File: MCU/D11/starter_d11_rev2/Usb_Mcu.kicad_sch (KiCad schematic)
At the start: 14 parts, among them J1 USB_A, J2 Data, J3 SWD-5, SW1 Reset, U1 PRTR5V0, U2 ATSAMD11C14A-SS, X1 ECS-2520MV-xxx-xx

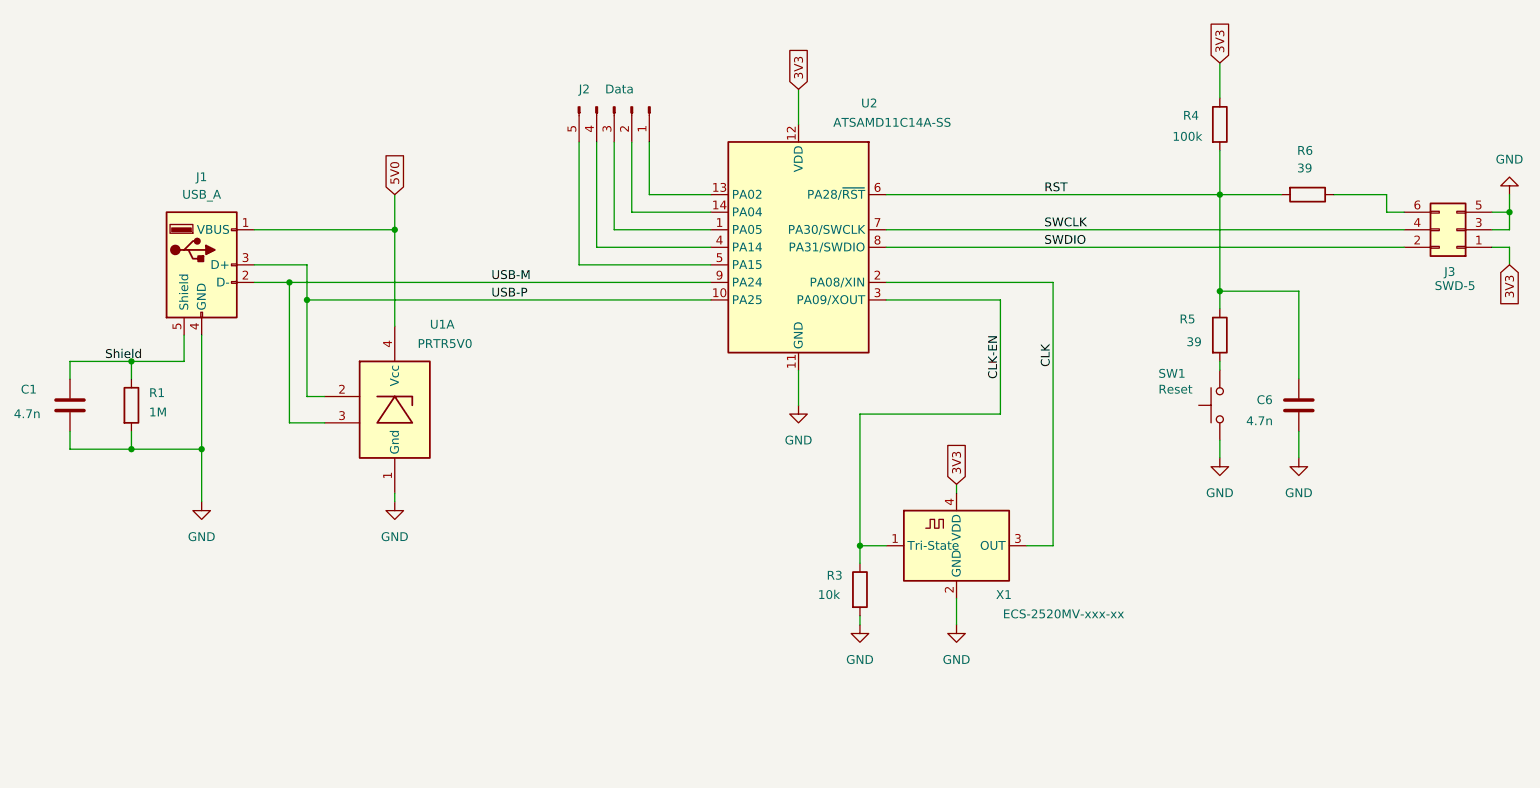
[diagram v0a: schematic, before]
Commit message: D11 schematics and PCB updates - printed prototype version
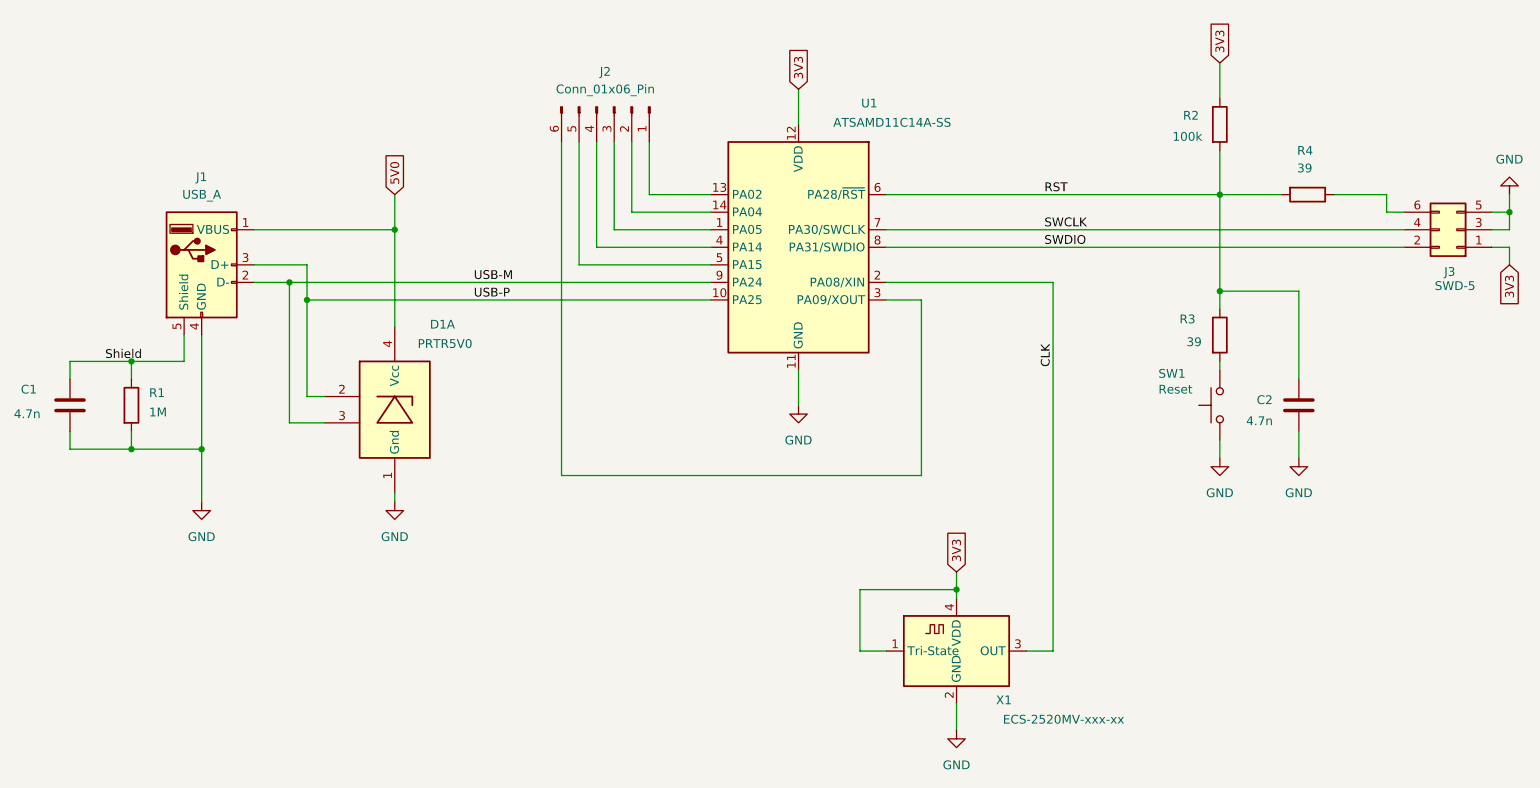
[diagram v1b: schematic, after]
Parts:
- removed J2: Data, Connector_PinHeader_2.54mm:PinHeader_1x05_P2.54mm_Vertical, symbol Connector:Conn_01x05_Pin
- removed R3: 10k, Resistor_SMD:R_0805_2012Metric_Pad1.20x1.40mm_HandSolder, symbol Device:R
- added J2: Conn_01x06_Pin, Connector_PinHeader_2.54mm:PinHeader_1x06_P2.54mm_Vertical, symbol Connector:Conn_01x06_Pin
- X1: footprint Oscillator:Oscillator_SMD_ECS_2520MV-xxx-xx-4Pin_2.5x2.0mm -> Secoh:ECS-2520MV
- renumbered C6 to C2, U1 to D1, R4 to R2, R5 to R3, R6 to R4, U2 to U1
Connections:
- net 3V3: now also X1.1 (Tri-State)
- net at U1.1 (PA05): now also J2.3 (Pin_3)
- net at U1.13 (PA02): now also J2.1 (Pin_1)
- net at U1.14 (PA04): now also J2.2 (Pin_2)
- net at U1.4 (PA14): now also J2.4 (Pin_4)
- net at U1.5 (PA15): now also J2.5 (Pin_5)
- net CLK-EN: no longer names the net of U1.3 (PA09/XOUT)
- net CLK-EN: now also J2.6 (Pin_6); no longer X1.1 (Tri-State)
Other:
- moved on the sheet: X1
